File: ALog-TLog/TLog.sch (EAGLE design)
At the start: 94 parts, among them IC1 ATMEGA644M, J6 5.5x2.1mm Barrel, Q1 220mA/50V/3.5Ω, Q5 MOSFET_PCH-IRLML2244, Q6 MOSFET_PCH-IRLML2244, Q7 MOSFET_PCH-IRLML2244, Q8 MOSFET-NCH-BSS138, Q9 MOSFET-NCH-BSS138, U2 FT231X-Q, U3 915MHz, U4 SX1509, X2 87832-14

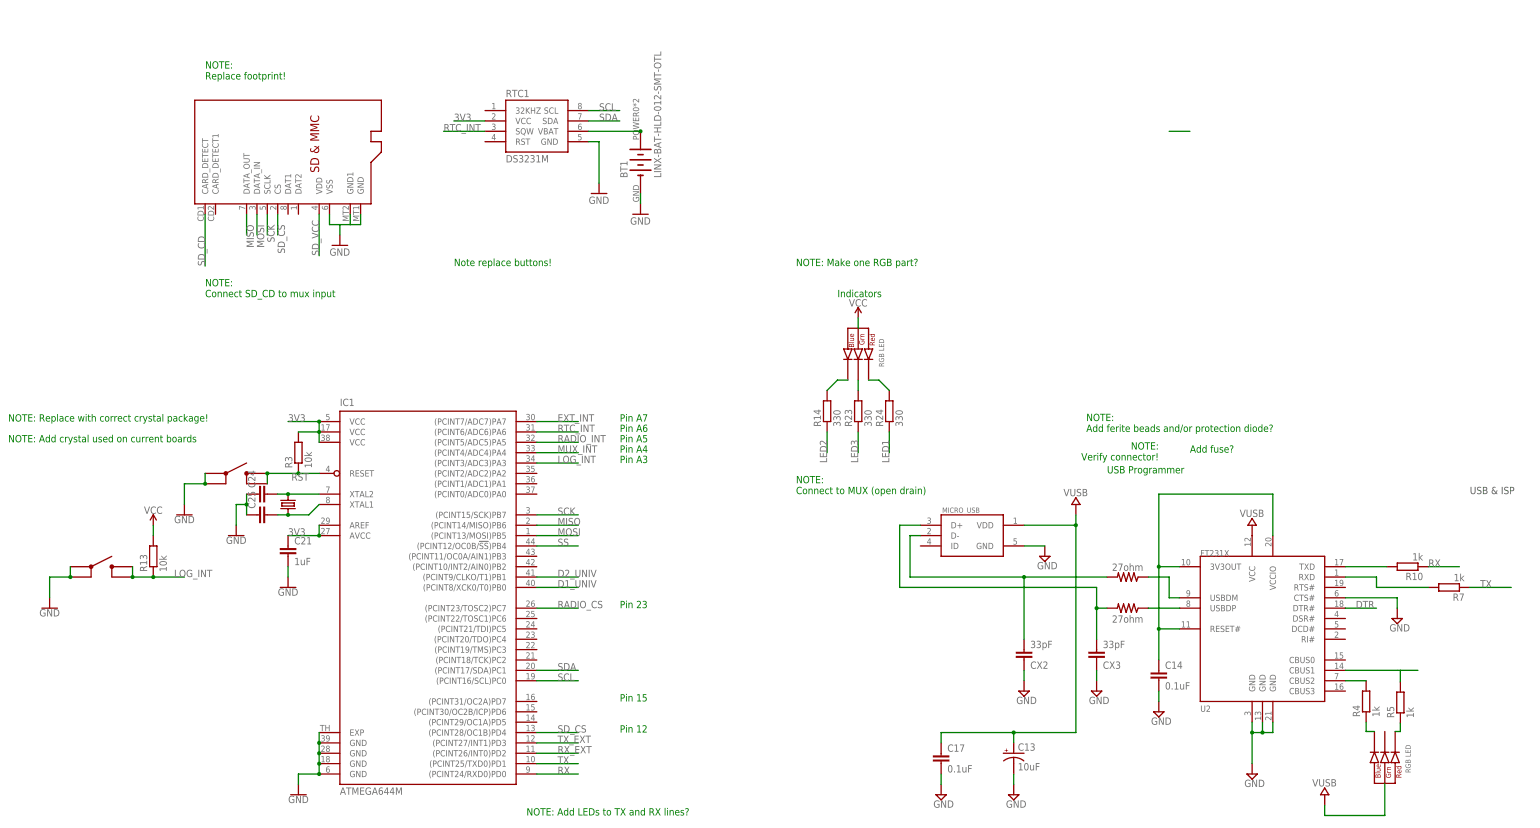
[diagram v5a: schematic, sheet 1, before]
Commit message: Added documentation so BOM auto-generates
Added attributes to parts to that when the BOM ULP is run, Digikey PNs are auto added along with other info.
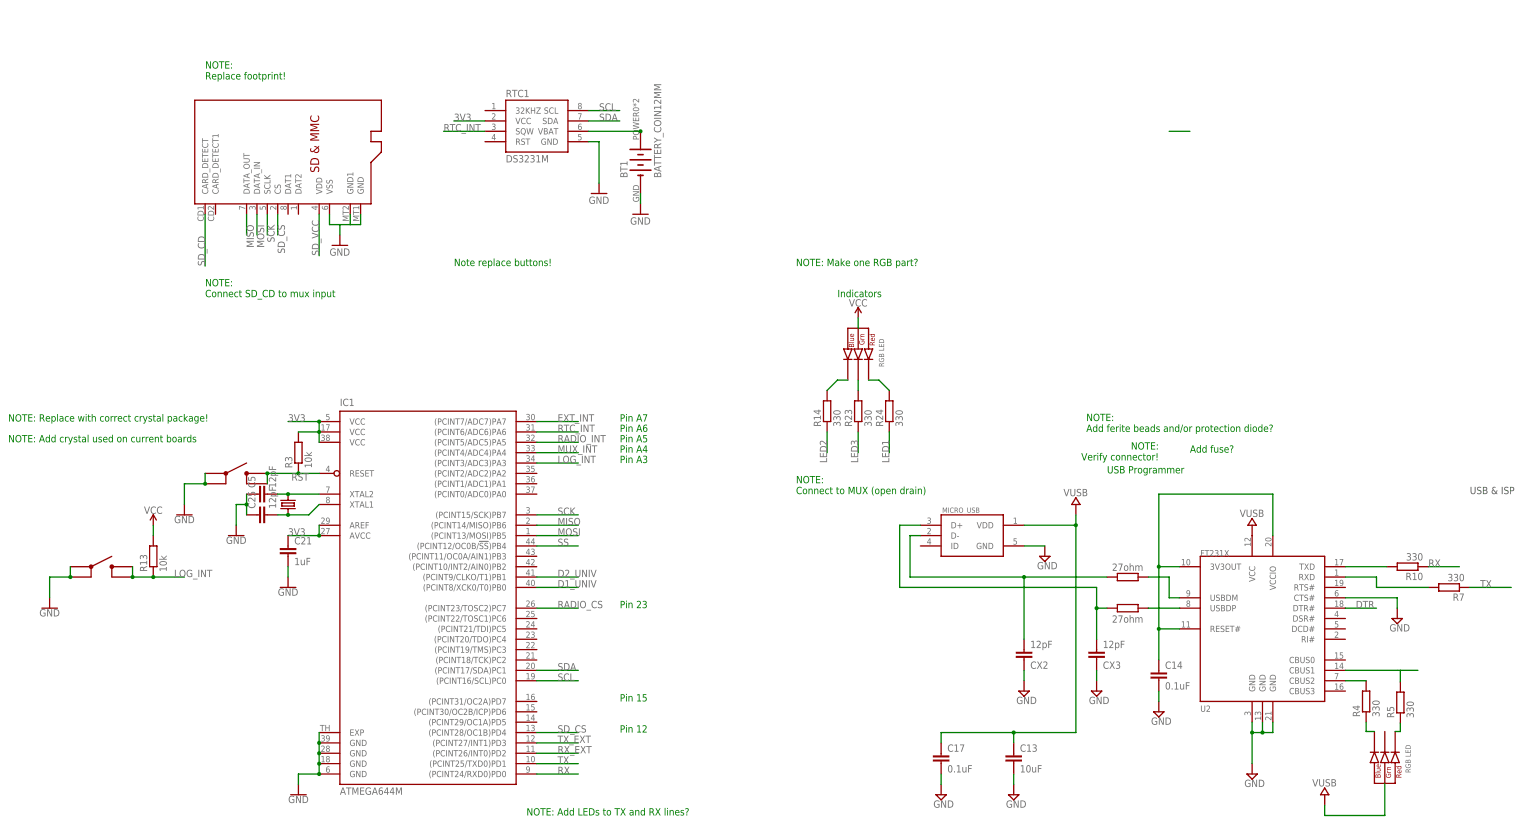
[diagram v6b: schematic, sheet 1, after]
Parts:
- BT1: value LINX-BAT-HLD-012-SMT-OTL -> BATTERY_COIN12MM; device awickert:LINX-BAT-HLD-012-SMT-OTL -> bschulz:BATTERY_COIN12MM
- C1, C10, C18, C22, C23: device rcl:C-EUC0603 -> bschulz:C-EU0.1UFC0603
- C11: device rcl:C-EUC0603 -> bschulz:C-EU12PFC0603
- C12, C29: DIGIKEY (none) -> 445-1854-1-ND; MF (none) -> TDK; MPN (none) -> CKCA43X7R1H103M100AA
- C13: device SparkFun-Passives:CAP_POL1206 -> bschulz:C-EU10UFC0805
- C14, C17: device resistor:C-EUC0603 -> bschulz:C-EU0.1UFC0603
- C19, C26, C27, C3: device rcl:C-EUC1206 -> bschulz:C-EU22UFC0805
- C2: device rcl:C-EUC0805 -> bschulz:C-EU10UFC0805
- C21: device rcl:C-EUC0603 -> bschulz:C-EU1UFC0603; DIGIKEY (none) -> 1276-6524-1-ND; MF (none) -> Samsung; MPN (none) -> CL10B105MO8NNWC
- C25, C5: value (none) -> 12pF; DIGIKEY (none) -> 1276-1254-1-ND; MF (none) -> Samsung; MPN (none) -> CL10C120JB8NNNC
- C4: device rcl:C-EUC0603 -> bschulz:C-EU2.2UFC0603
- CX2, CX3: value 33pF -> 12pF; device resistor:C-EUC0603 -> bschulz:C-EU12PFC0603
- D+, D-: device rcl:R-US_R0603 -> bschulz:R-EU_27R0603
- F1, F2: value 6V/0.5A -> PPTC_HALF-AMP; device SparkFun-Fuses:PPTC_HALF-AMP -> bschulz:PPTC_HALF-AMP
- ISP2: DIGIKEY (none) -> 609-3234-ND; MF (none) -> Amphenol; MPN (none) -> 67997-206HLF
- J10, J5, J8, J9: DIGIKEY (none) -> ED2735-ND; MF (none) -> On Shore Technology; MPN (none) -> OSTTE100104
- J4: device SparkFun-Connectors:JST_2MM_MALE -> bschulz:JST_2MM_MALE
- J6: device SparkFun-Connectors:POWER_JACKSMD -> bschulz:POWER_JACKSMD
- L2: DIGIKEY (none) -> 732-10754-1-ND; MF (none) -> Wurth; MPN (none) -> 74404043022A
- Q1: value 220mA/50V/3.5Ω -> MOSFET-NCH-BSS138; device SparkFun-DiscreteSemi:MOSFET-NCH-BSS138 -> bschulz:MOSFET-NCH-BSS138
- R1: device rcl:R-EU_R0603 -> bschulz:R-EU_R0603; DIGIKEY (none) -> 311-143KHRCT-ND; MF (none) -> Yageo; MPN (none) -> RC0603FR-07143KL
- R10, R4, R7: value 1k -> 330; device rcl:R-EU_R0603 -> bschulz:R-EU_330R0603; MPN (none) -> RC0603FR-07330RL
- R11, R12, R15, R18, R19, R20, R21, R22, R26, R27, R28, R3, R42, R43, R46, R47, R8, R9: device rcl:R-EU_R0603 -> bschulz:R-EU_10KR0603
- R13, R6: device resistor:R-EU_R0603 -> bschulz:R-EU_10KR0603
- R14, R23, R24: device resistor:R-EU_R0603 -> bschulz:R-EU_330R0603; MPN (none) -> RC0603FR-07330RL
- R16, R17: DIGIKEY (none) -> 1276-6358-1-ND; MF (none) -> Samsung; MPN (none) -> CIC10P471NC
- R2: device rcl:R-EU_R0603 -> bschulz:R-EU_R0603; DIGIKEY (none) -> 311-953KHRCT-ND; MF (none) -> Yageo; MPN (none) -> RC0603FR-07953KL
- R5: value 1k -> 330; device rcl:R-EU_R0603 -> bschulz:R-EU_330R0603; DIGIKEY (none) -> 311-330HRCT-ND; MF (none) -> Yageo; MPN (none) -> RC0603FR-07330RL
- U$1: value CRYSTAL_5X3.2_2LEAD -> CRYSTALTXC_8MHZ; device bschulz:CRYSTAL_5X3.2_2LEAD -> bschulz:CRYSTALTXC_8MHZ
- U$4: value TPS62172 -> TPS62172-Q1; device SparkFun-IC-Power:TPS62172 -> bschulz:TPS62172-Q1
- U$5, U$9: value SKRPABE010 -> SWITCHC&K_400GF; device bschulz:SKRPABE010 -> bschulz:SWITCHC&K_400GF
- U$6: MF (none) -> UBlox
- U$8: DIGIKEY (none) -> 732-11310-1-ND; MF (none) -> Wurth; MPN (none) -> 78438356010
- U2: device FT231X:FT231X-Q -> bschulz:FT231X-Q
- U6: device microbuilder:VREG_TPS63060/1 -> bschulz:TPS63060
- X1: device adafruit:SMACONNECTOR_EDGE -> bschulz:SMA_EDGE
- X2: DIGIKEY (none) -> WM18702-ND; MF (none) -> Molex; MPN (none) -> 0791091006
- renumbered C24 to C5
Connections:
- net GND: now also C13.2; no longer C13.-
- net VUSB: now also C13.1; no longer C13.+

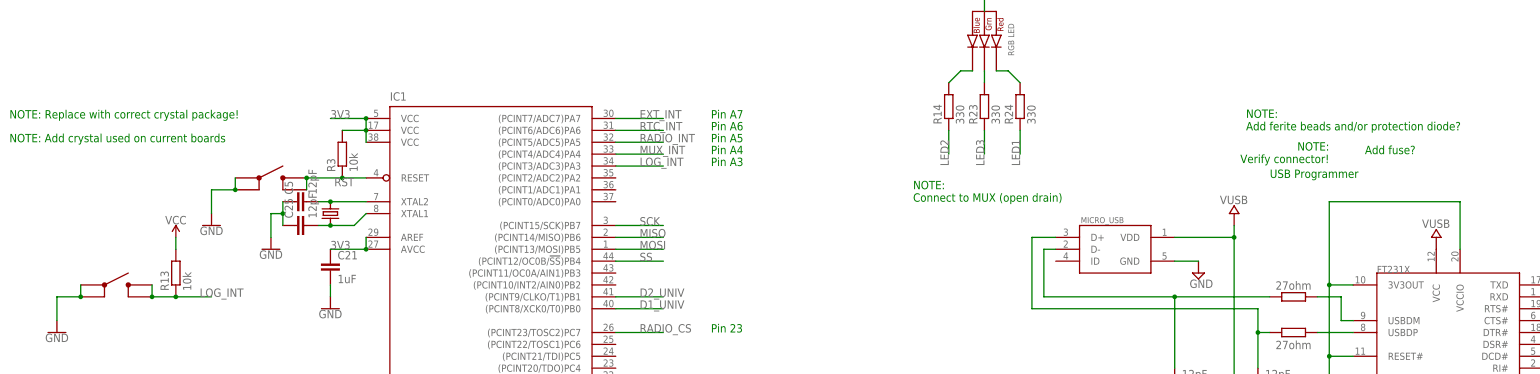
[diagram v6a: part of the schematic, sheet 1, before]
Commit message: Changes from round #1 of board testing
Changed capacitor sizes, fixed ADC COM pin, fixed DTR pin, connected 5V and VUSB, put converters in series, changed resistor divider values for switchmode regulator
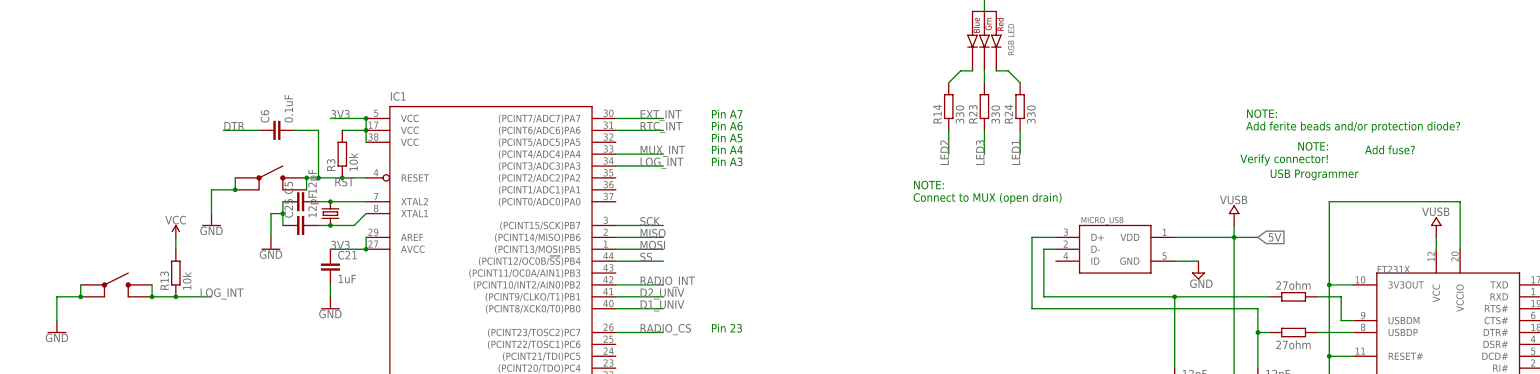
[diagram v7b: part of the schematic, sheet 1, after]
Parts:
- added C6: 0.1uF, bschulz:C-EU0.1UFC0603
- added R25, R29: 10k, bschulz:R-EU_10KR0603
- C4: device bschulz:C-EU2.2UFC0603 -> bschulz:C-EU10UFC0805
- L2: value 10uH -> 2.2uF; device bschulz:INDUCTORLQS_4X4 -> bschulz:INDUCTOR0806; DIGIKEY 732-10754-1-ND -> 732-5709-1-ND; MPN 74404043022A -> 74438343022
- R1: value 143k -> 111k
- R2: value 953k -> 1M
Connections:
- removed net VUSB: C13.1, C17.1, MICRO_USB.VDD, U$16.ANODE, U2.VCC
- new net COM: R25.1, R29.2, U$7.COM
- net 5V: now also C13.1, C17.1, C4.1, MICRO_USB.VDD, R25.2, U$16.ANODE, U$4.EN, U$4.VIN, U2.VCC
- net BATT+: no longer C4.1, U$4.EN, U$4.VIN
- net DTR: now also C6.1
- net GND: now also R29.1; no longer U$7.COM
- net RADIO_INT: now also IC1.(PCINT10/INT2/AIN0)PB2; no longer IC1.(PCINT5/ADC5)PA5
- net RST: now also C6.2
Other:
- note removed: "NOTE: Add crystal used on current boards"
- note removed: "NOTE: Replace with correct crystal package!"

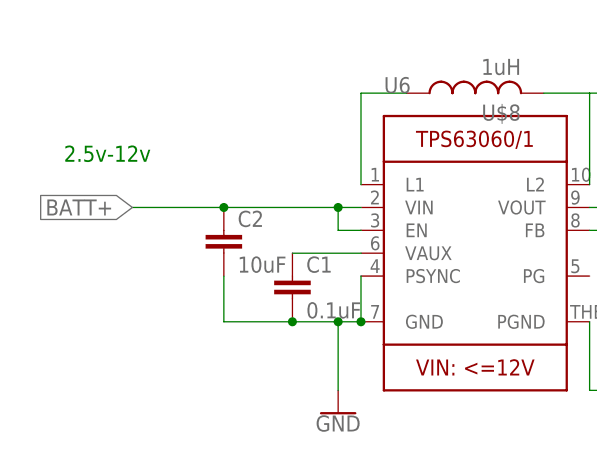
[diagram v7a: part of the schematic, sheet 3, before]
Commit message: Fixed Switchmode Converter Errors
Attempted to fix problems with switchmode 5v convetred by adding bottom layer ground plane, and generally improving top planes. In order to attempt to improve overall noise, analog plane was added. Also added control for PSYNC line on 5v converter to GPIO on IO expander
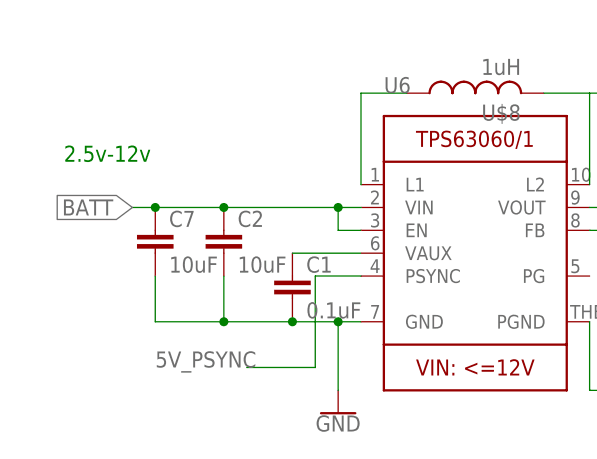
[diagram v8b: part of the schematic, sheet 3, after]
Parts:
- added C7: 10uF, bschulz:C-EU10UFC0805
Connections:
- removed net BATT+: C2.1, J4.+, J6.PWR, R46.2, U6.EN, U6.VIN
- new net 5V_PSYNC: U4.I/O[0], U6.PSYNC
- new net BATT: C2.1, C7.1, J4.+, J6.PWR, R46.2, U6.EN, U6.VIN
- net 3V3: now also U$10.VIN
- net 5V: no longer U$10.VIN
- net GND: now also C7.2; no longer U6.PSYNC
